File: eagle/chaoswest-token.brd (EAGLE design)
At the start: 44 x 50.7 mm, 19 parts, among them J1 Amphenol 10118194, Q1 Si1967DH, SW1 AYZ0102AGRLC, U1 MCP73832T-2ACI/OT

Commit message: current status of board (front side quasi final) and some more dxf / xml files added
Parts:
- removed J1: Amphenol 10118194, we-con:USB-MICROB-10118194
- added U$1, U$2: EMPTY_SIGNAL, extra:SMALLSPOT
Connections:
- removed net USB-DM: J1.D-
- removed net USB-DP: J1.D+
- new net N$27: U$1.X, U$2.X
- net GND: no longer J1.GND
- net N$22: no longer J1.VBUS
- net N$59: no longer J1.SHLD1, J1.SHLD2, J1.SHLD3, J1.SHLD4, J1.SHLD5, J1.SHLD6, J1.SHLD7, J1.SHLD8
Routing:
- net N$27: track 0.00 -> 159.5 mm
- net N$2: track 28.8 -> 0.00 mm, vias 2 -> 0
- net N$81: track 0.00 -> 5.54 mm
- net N$37: track 0.00 -> 4.36 mm
- net N$110: track 0.00 -> 4.36 mm
- net N$84: track 0.00 -> 4.02 mm
- net N$65: track 0.00 -> 4.02 mm
- net N$63: track 0.00 -> 3.68 mm
- net N$39: track 0.00 -> 3.68 mm
- net N$107: track 0.00 -> 3.68 mm
- net N$111: track 0.00 -> 3.47 mm
- net N$83: track 0.00 -> 3.44 mm
- net N$67: track 0.00 -> 3.44 mm
- net N$69: track 0.00 -> 3.13 mm
- net N$78: track 0.00 -> 3.13 mm
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- removed copper zone on layer 1, net N$1

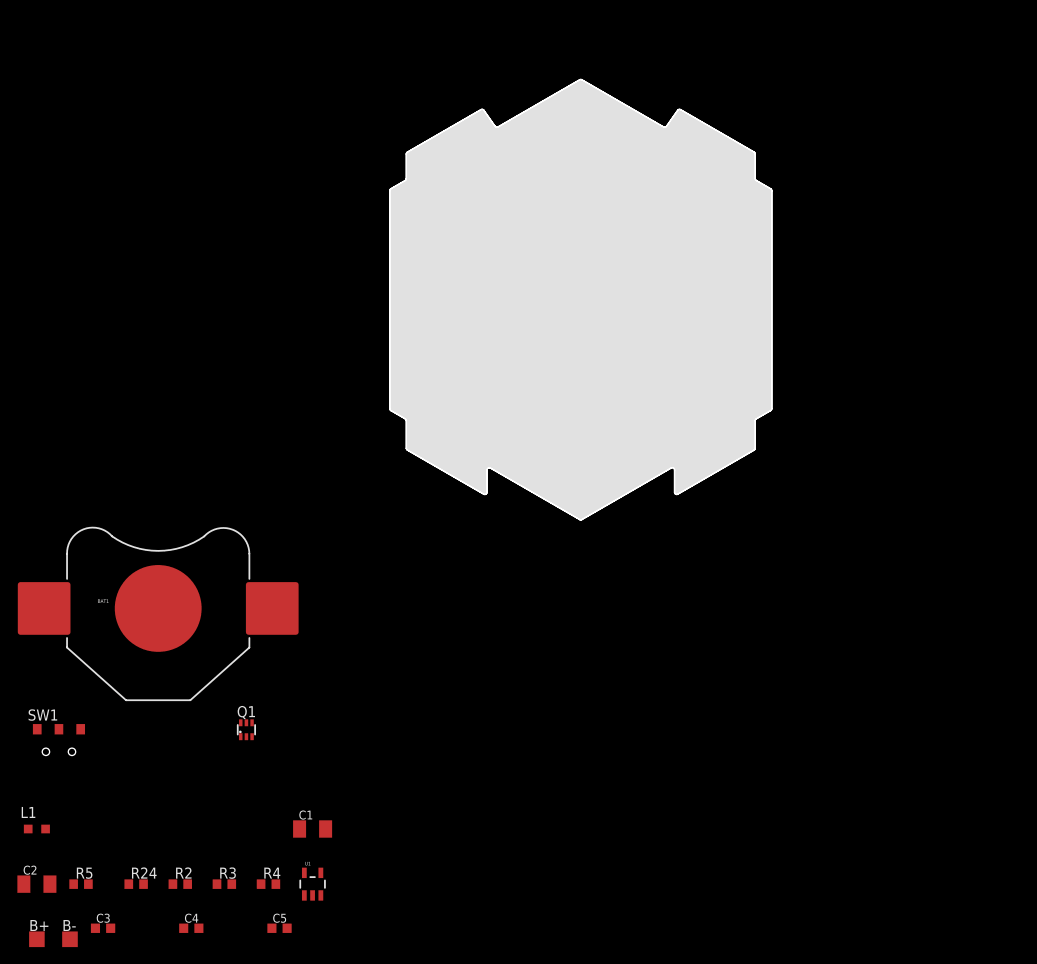
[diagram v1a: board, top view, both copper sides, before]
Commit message: schematic should be mostly done, routing is in process, 42 airwires left
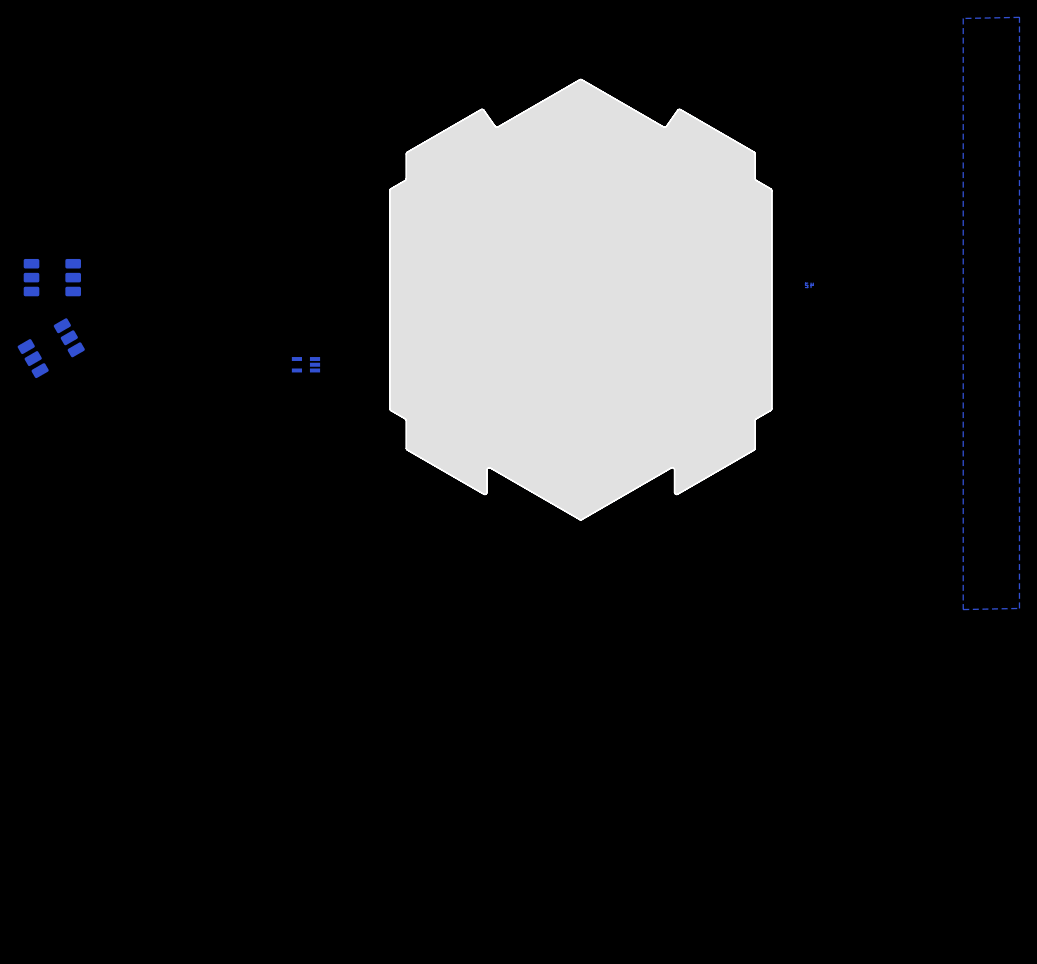
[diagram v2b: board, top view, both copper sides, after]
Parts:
- removed R2: 4k7, rcl:R0603
- removed R24: 47k, rcl:R0603
- removed R3: 10k, rcl:R0603
- added C6: 100n, we-rcl:C0805
- added D1, D2: 3V6, we-rcl:SOD123
- added J1: (no value), Molex-47346-0001:MOLEX_47346-0001
- added J2: CON_HEADER_PRG_AVR_ICSP-SMD, dp_devices:M2X3_SMD
- added LED2, LED3, LED4, LED5, LED6: WS2813, extra:WS2813
- added R1, R6: 68, we-rcl:C0805
- added R7: 2k2, we-rcl:C0805
- added SJ1, SJ3, SJ4: (no value), jumper:SJ_2
- added TP1: DO, testpad:TP09SQ
- added TP2: BO, testpad:TP09SQ
- added TP3: GND, testpad:TP09SQ
- added U$3, U$4: EMPTY_SIGNAL, extra:SMALLSPOT
- added U2: ATTINY85V-10SU, Atmel-ATTINY85V-10SU:SOIC127P798X216-8N
- added U3: MCP9700AT-E/LT, Microchip_By_element14_Batch_1:SOT65P210X110-5N
- BAT1: device Keystone-3002:BATTCON_20MM -> extra:BATTCON_20MM
- C1, C2: device rcl:C1206K -> we-rcl:C0805
- C3, C4, C5: device rcl:C0603K -> we-rcl:C0805
- L1: device rcl:L2012C -> we-rcl:C0805
- R4, R5: device rcl:R0603 -> we-rcl:C0805
- SW1: value AYZ0102AGRLC -> SSAJ120100; device C&K-Switch:AYZ0102AGRLC -> extra:SSAJ120100
- moved C2 101.3 mm to (33.8, 26.8), flipped to the bottom, turned to 90 degrees
- moved SW1 101.0 mm to (42.7, 34.0), flipped to the bottom, turned to 270 degrees
- moved R5 98.8 mm to (41.7, 19.7), flipped to the bottom, turned to 270 degrees
- moved L1 96.9 mm to (35.1, 25.0), flipped to the bottom, turned to 90 degrees
- moved C3 95.3 mm to (31.5, 23.1), flipped to the bottom, turned to 270 degrees
- moved B+ 89.7 mm to (6.35, 28.2), flipped to the bottom
- moved B- 89.2 mm to (9.14, 28.2), flipped to the bottom
- moved C5 84.6 mm to (41.7, 17.8), flipped to the bottom, turned to 90 degrees
- moved C4 84.1 mm to (25.4, 21.8), flipped to the bottom, turned to 90 degrees
- moved Q1 75.1 mm to (37.0, 28.6), flipped to the bottom, turned to 270 degrees
- moved C1 73.3 mm to (35.1, 23.1), flipped to the bottom, turned to 90 degrees
- moved U1 73.2 mm to (29.5, 20.4), flipped to the bottom, turned to 90 degrees
- moved R4 73.2 mm to (26.3, 19.2), flipped to the bottom
- moved BAT1 65.5 mm to (22.0, 33.7), flipped to the bottom
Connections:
- removed net +3V3: R24.2
- removed net CHG-STAT: R24.1, U1.1
- removed net N$22: C1.1, L1.1
- removed net N$23: C2.1, C3.1, L1.2, Q1.2, Q1.3, R2.2, U1.4
- removed net N$31: B+.TP, BAT1.+2, C4.1, SW1.3, U1.3
- removed net N$6 (its old number): LED1.A
- removed net USB-SENSE: R2.1, R3.2
- new net +5V: C2.1, C3.1, L1.2, Q1.2, Q1.3, R7.2, U1.4
- new net LED1: LED1.K, SJ1.2
- new net LED2: SJ3.2, U$3.X
- new net LED3: SJ4.2, U$4.X
- new net N$2: LED2.3, LED3.4, LED4.6
- new net N$35: LED4.3, LED5.4, LED6.6
- new net N$42: LED5.3, LED6.4, TP2.TP
- new net N$43: LED6.3, TP1.TP
- new net PB0/MOSI/LED1: J2.4, SJ1.1, U2.5
- new net PB1/MISO/LED2/WS2813: J2.1, LED2.4, LED3.6, SJ3.1, U2.6
- new net PB2/SCK/TEMP: J2.3, U2.7, U3.3
- new net PB3/USB-DM: R1.2, U2.2
- new net PB4/USB-DP: R6.2, U2.3
- new net PB5/RESET/LED3: J2.5, SJ4.1, U2.1
- new net USB-DM: D2.C, J1.2, R1.1, R7.1
- new net USB-DP: D1.C, J1.3, R6.1
- new net VBAT: B+.TP, BAT1.+1, BAT1.+2, C4.1, SW1.1, U1.3
- new net VBUS: C1.1, J1.1, L1.1
- net GND: now also C6.2, D1.A, D2.A, J1.5, J2.6, LED2.5, LED3.5, LED4.5, LED5.5, LED6.5, SJ1.3, SJ3.3, SJ4.3, TP3.TP, U2.4, U3.2; no longer R3.1
- net N$59: now also J1.M1, J1.M2, J1.M3, J1.M4, J1.M5, J1.M6
- net N$7: now also LED3.3, LED4.4, LED5.6; no longer LED1.K
- net VCC: now also C6.1, J2.2, LED1.A, LED2.2, LED3.2, LED4.2, LED5.2, LED6.2, SW1.3, U2.8, U3.4; no longer SW1.1
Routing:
- net GND: track 0.00 -> 141.0 mm, vias 0 -> 6
- net VCC: track 0.00 -> 69.2 mm, vias 0 -> 1
- net N$5: track 41.3 -> 0.00 mm, vias 2 -> 0
- net N$2: track 0.00 -> 34.1 mm
- net N$4: track 31.2 -> 1.02 mm, vias 2 -> 0
- net VBAT: track 0.00 -> 25.0 mm
- net +5V: track 0.00 -> 23.7 mm
- net N$6 (its old number): track 19.0 -> 0.00 mm, vias 1 -> 0
- net N$59: track 0.00 -> 15.5 mm
- net N$7: track 15.5 -> 0.00 mm, vias 1 -> 0
- net LED1: track 0.00 -> 15.5 mm, vias 0 -> 1
- net PB1/MISO/LED2/WS2813: track 0.00 -> 13.8 mm
- net USB-DM: track 0.00 -> 12.9 mm
- net USB-DP: track 0.00 -> 11.8 mm
- net N$35: track 0.00 -> 9.29 mm
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- added copper zone on layer 16, net GND
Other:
- board text added: "make vias here isolated from the battery!"

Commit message: routing finished, single layer layout
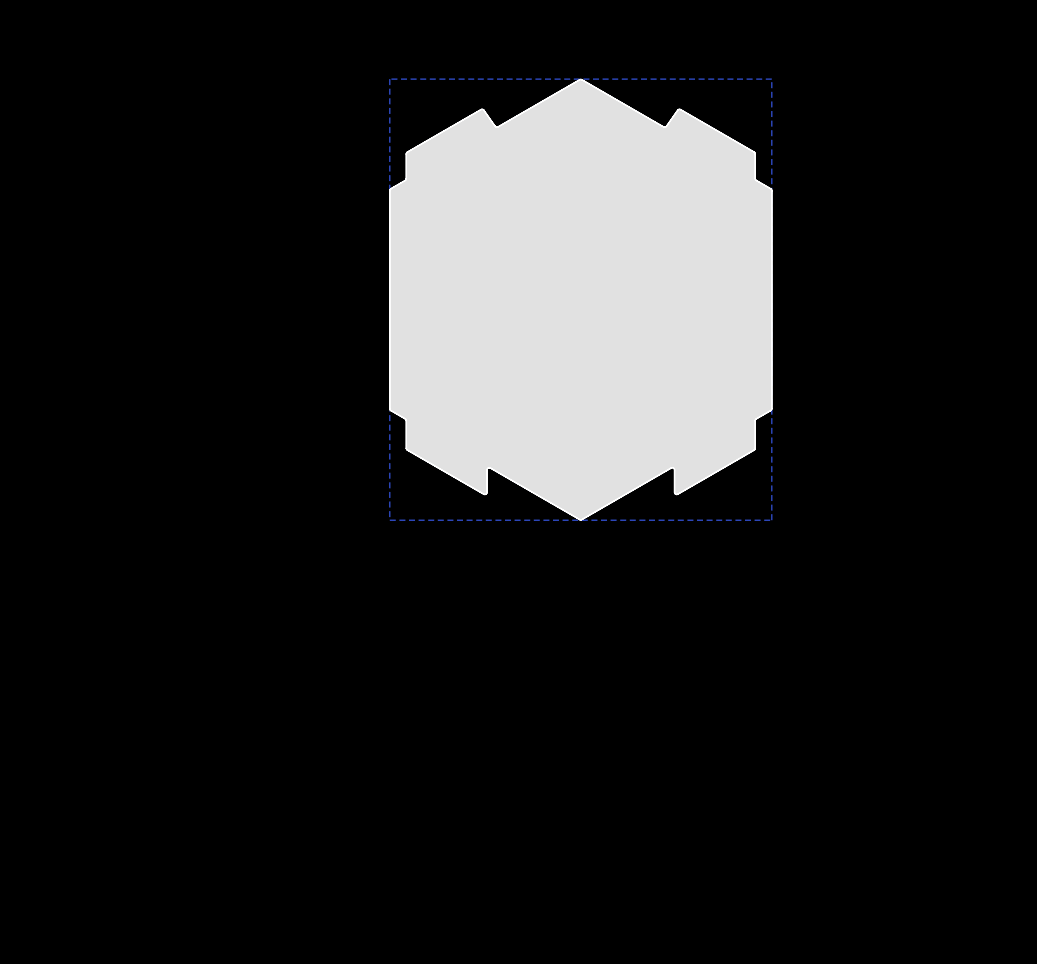
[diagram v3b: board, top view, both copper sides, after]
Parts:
- J1: value (none) -> USB
- J2: value CON_HEADER_PRG_AVR_ICSP-SMD -> ISP
- moved LED3 47.3 mm to (7.32, 9.96), turned to 30 degrees
- moved LED4 43.2 mm to (4.27, 25.4), turned to 90 degrees
- moved U3 15.0 mm to (5.33, 17.9), turned to 270 degrees
- moved TP2 7.39 mm to (34.5, 38.2)
- moved TP1 6.75 mm to (35.7, 37.6)
- moved TP3 6.32 mm to (33.4, 38.9)
- moved B+ 5.39 mm to (11.6, 26.8)
- moved J2 4.86 mm to (12.2, 19.6), turned to 180 degrees
- moved SJ1 4.32 mm to (21.6, 17.1)
- moved C6 2.80 mm to (19.4, 13.1)
- moved B- 1.40 mm to (9.02, 26.8)
- moved LED2 0.78 mm to (36.7, 9.96)
- moved LED6 0.78 mm to (36.7, 40.5)
- moved LED5 0.78 mm to (7.32, 40.5)
- moved C3 0.63 mm to (30.9, 23.1)
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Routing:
- net VCC: track 69.2 -> 231.2 mm, vias 1 -> 3
- net GND: track 141.0 -> 269.1 mm, vias 6 -> 4
- net PB1/MISO/LED2/WS2813: track 13.8 -> 71.2 mm
- net N$35: track 9.29 -> 61.4 mm
- net N$7: track 0.00 -> 43.5 mm
- net PB0/MOSI/LED1: track 0.00 -> 39.4 mm
- net N$42: track 6.21 -> 41.1 mm
- net PB2/SCK/TEMP: track 0.00 -> 32.5 mm
- net N$2: track 34.1 -> 64.7 mm
- net PB5/RESET/LED3: track 0.00 -> 25.3 mm
- net VBAT: track 25.0 -> 33.0 mm
- net N$43: track 8.01 -> 2.88 mm
- net LED1: track 15.5 -> 18.9 mm
- net +5V: track 23.7 -> 20.5 mm
- net LED2: track 5.03 -> 7.91 mm
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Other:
- board text removed: "make vias here isolated from the battery!"
